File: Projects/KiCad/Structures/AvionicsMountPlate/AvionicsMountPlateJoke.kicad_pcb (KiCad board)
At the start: 2 copper layers, 140 x 140 mm, 41 parts

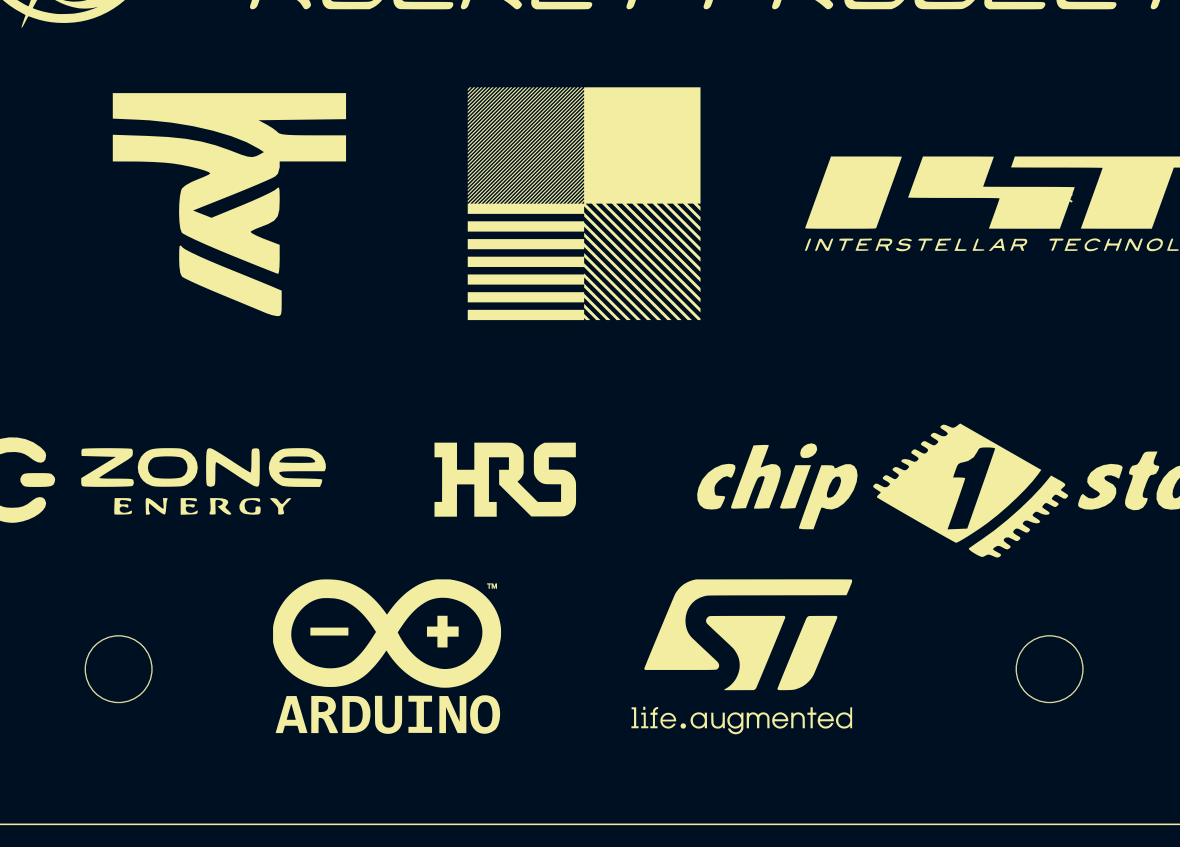
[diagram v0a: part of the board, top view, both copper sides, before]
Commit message: 許されざる基板を追加
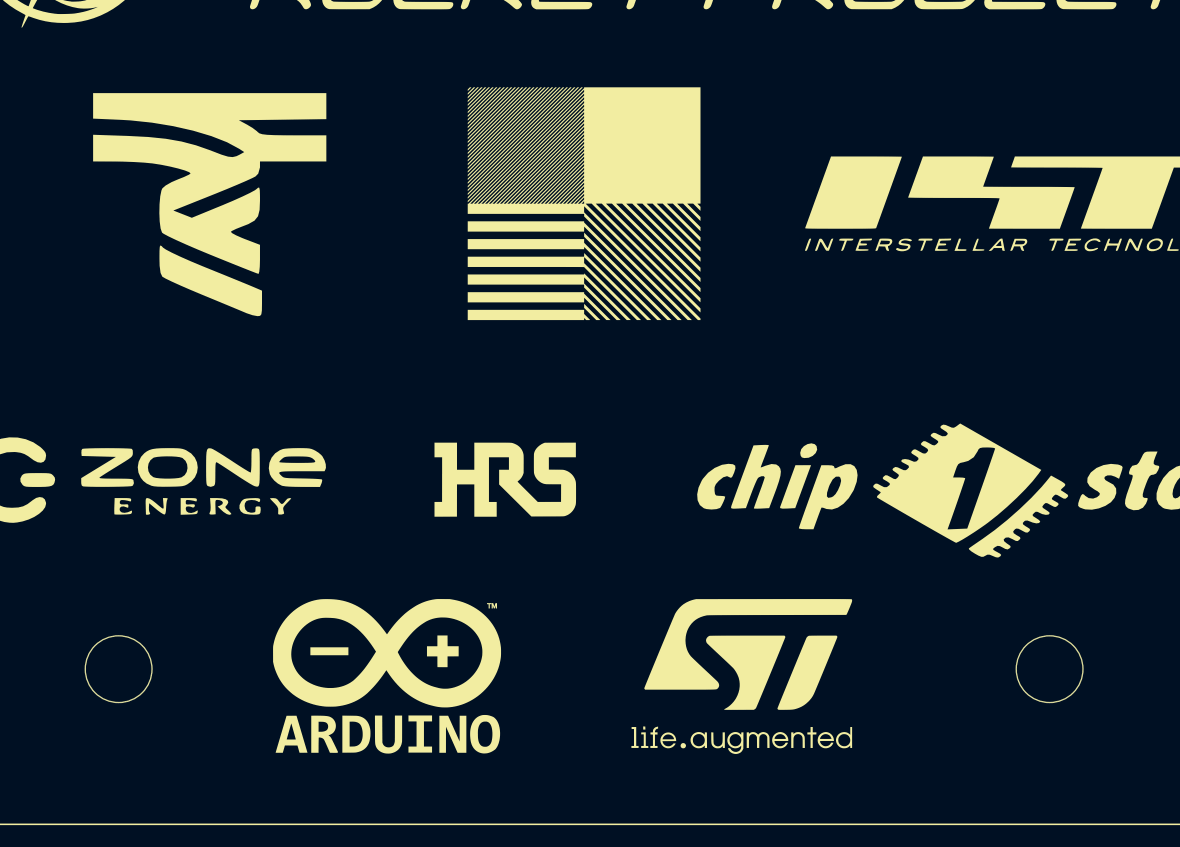
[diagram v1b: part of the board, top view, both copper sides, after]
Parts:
- moved G*** 1.27 mm to (159.8, 117.9)
- moved G*** 1.27 mm to (125.5, 87.4)
- moved G*** 1.27 mm to (136.9, 117.9)
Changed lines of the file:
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@@
     (at 178.828059 87.388059)
     (attr board_only exclude_from_pos_files exclude_from_bom)
-    (fp_text reference "G***" (at 0 0) (layer "F.SilkS")
+    (fp_text reference "G***" (at 0 0) (layer "F.SilkS") hide
         (effects (font (size 1.5 1.5) (thickness 0.3)))
     )
@@
   )
   (footprint "LOGO" (layer "F.Cu")
-    (at 159.778059 116.598059)
+    (at 159.778059 117.868059)
     (attr board_only exclude_from_pos_files exclude_from_bom)
     (fp_text reference "G***" (at 0 0) (layer "F.SilkS") hide
@@
   )
   (footprint "LOGO" (layer "F.Cu")
-    (at 126.758059 87.388059)
+    (at 125.488059 87.388059)
     (attr board_only exclude_from_pos_files exclude_from_bom)
     (fp_text reference "G***" (at 0 0) (layer "F.SilkS") hide
@@
   )
   (footprint "LOGO" (layer "F.Cu")
-    (at 136.918059 116.598059)
+    (at 136.918059 117.868059)
     (attr board_only exclude_from_pos_files exclude_from_bom)
     (fp_text reference "G***" (at 0 0) (layer "F.SilkS") hide

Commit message: 許されざる基板を修正
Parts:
- added G***: LOGO, LOGO, F.Cu at (133.1, 106.4)
- added G***: LOGO, LOGO, F.Cu at (166.1, 106.4)
- added REF**: MountingHole_5.5mm, MountingHole:MountingHole_5.5mm, F.Cu at (200.4, 87.4)
- added REF**: MountingHole_5.5mm, MountingHole:MountingHole_5.5mm, F.Cu at (149.6, 36.6)
- added REF**: MountingHole_5.5mm, MountingHole:MountingHole_5.5mm, F.Cu at (98.8, 87.4)
- moved G*** 24.1 mm to (161.0, 117.9)
- moved G*** 20.3 mm to (139.5, 117.9)
- moved G*** 9.92 mm to (115.3, 97.5)
- moved G*** 8.03 mm to (142.0, 97.5)
- moved G*** 7.62 mm to (176.3, 98.8)
- moved G*** 3.59 mm to (176.3, 84.8)
- moved G*** 2.54 mm to (149.6, 84.8)
- moved G*** 2.54 mm to (125.5, 84.8)

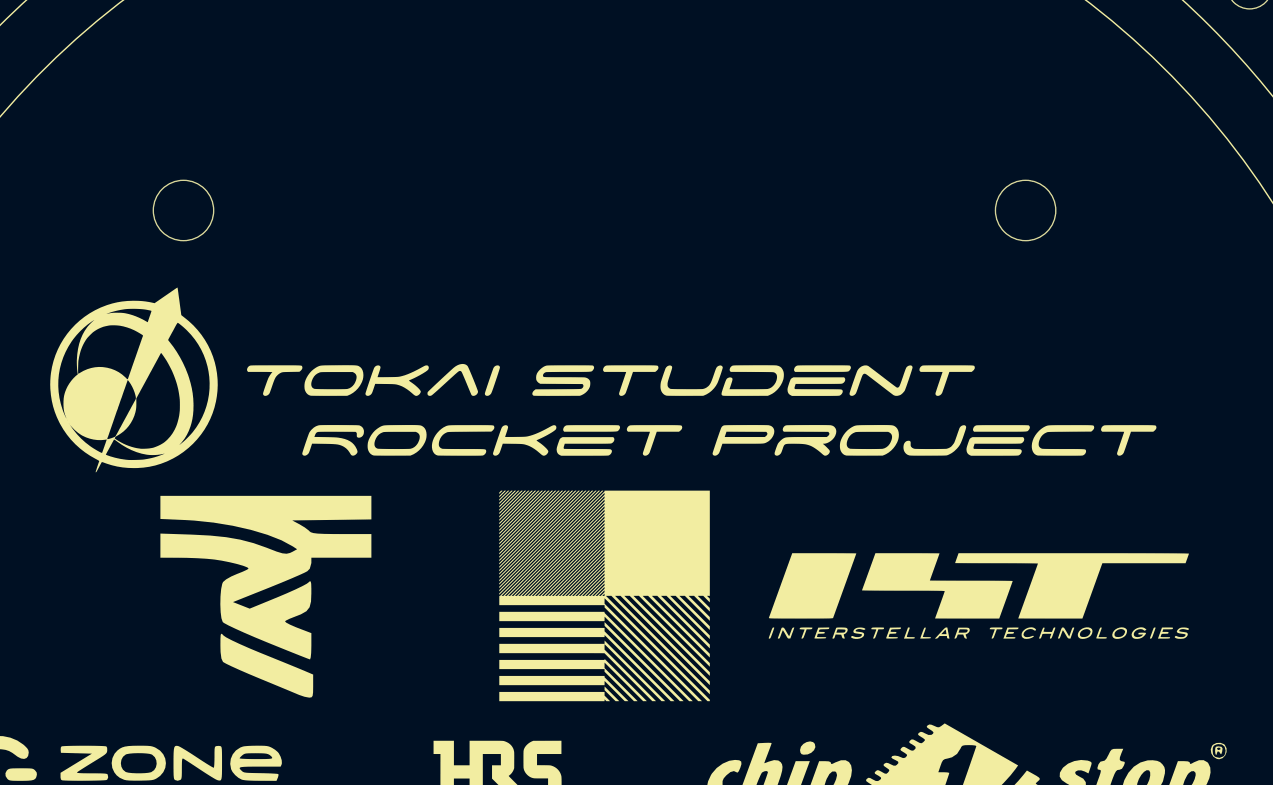
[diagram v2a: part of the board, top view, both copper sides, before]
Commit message: コネクタ位置を揃えた
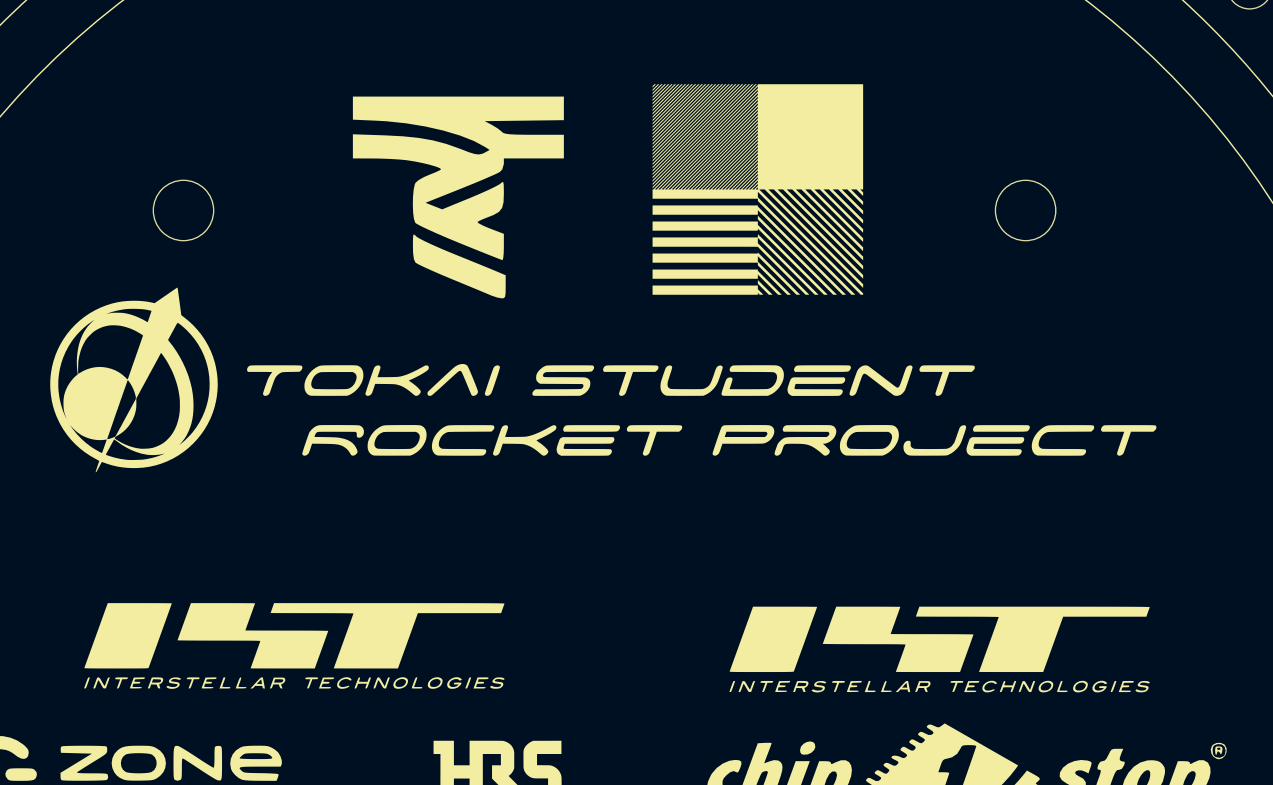
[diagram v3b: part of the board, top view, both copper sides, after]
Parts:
- added G***: LOGO, LOGO, F.Cu at (173.5, 88.7)
- moved G*** 48.9 mm to (127.5, 88.4)
- moved G*** 31.6 mm to (139.2, 56.4)
- moved G*** 30.9 mm to (160.5, 55.9)
